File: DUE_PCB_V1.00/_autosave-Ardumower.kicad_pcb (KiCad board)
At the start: 2 copper layers, 169.4 x 95.9 mm, 73 parts, among them J1 9V IN, J10 Sonar_R, J11 Sonar_C, J12 Sonar_L, J13 P_Right, J15 Button, J16 Button, J17 Button, J18 Button, J19 P_Left, J2 I2C0_1, J20 Remote, J21 PCB_2, J22 3.3V, J23 GND, J24 RX & TX, J25 5V IN, J26 Motor Left, J27 Cutter Motor, J28 Motor Right, J29 3.3V IN, J3 I2C0_2, J30 I2C1_2, J4 I2C1_1, J5 Bumper, J6 Drop_Left, J7 Drop_Right, J8 Tilt, J9 Rain, U1 MC33926, U2 MC33926

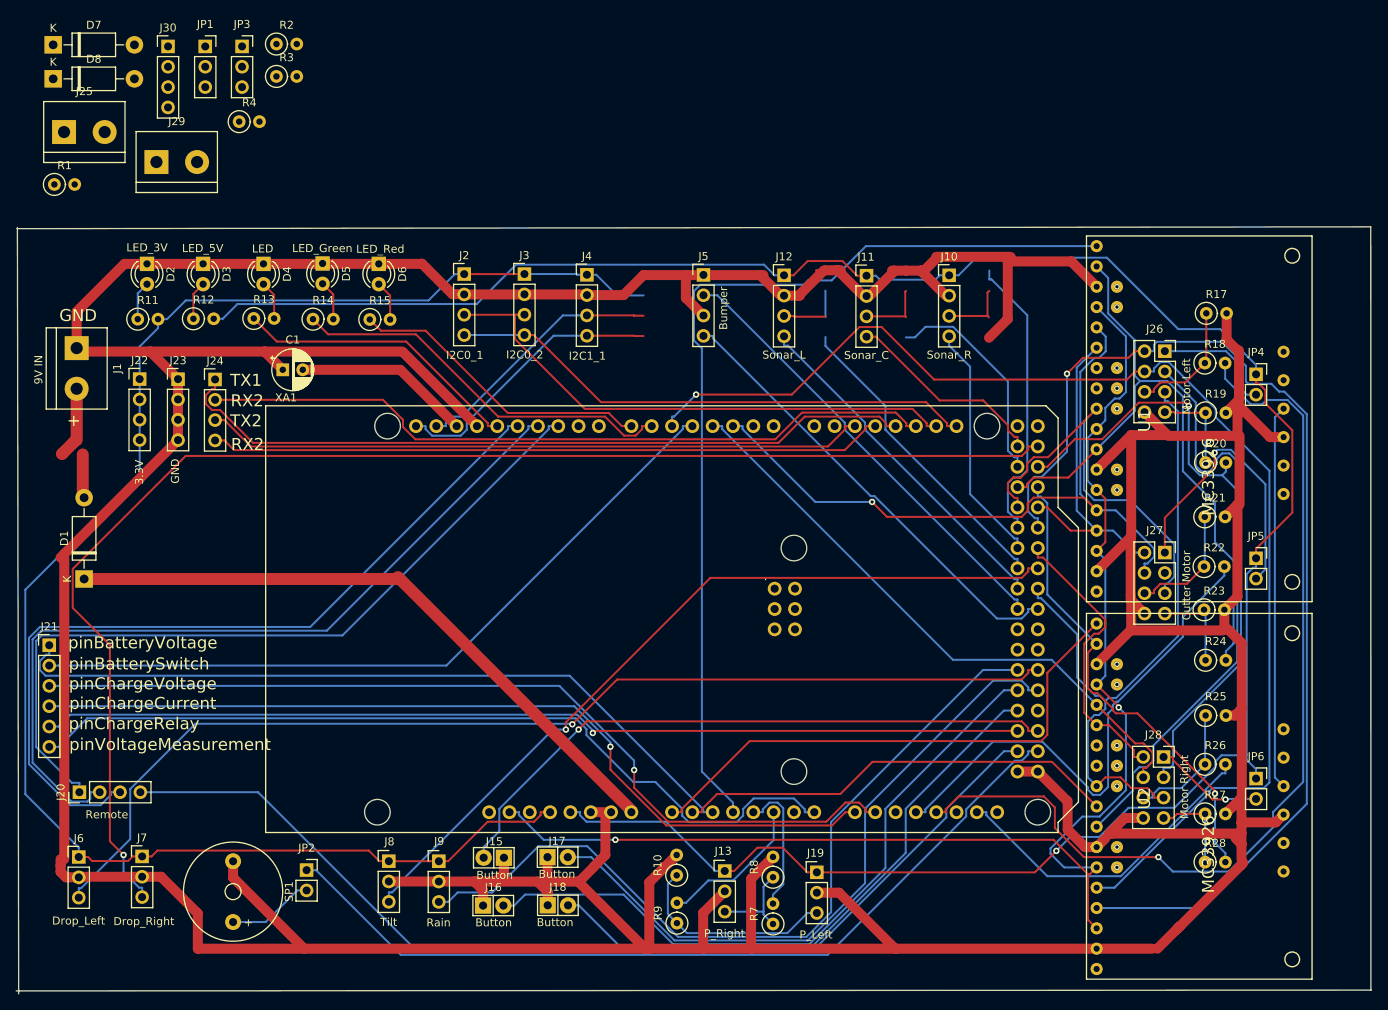
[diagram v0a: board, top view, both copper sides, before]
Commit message: Add Mounting Hole
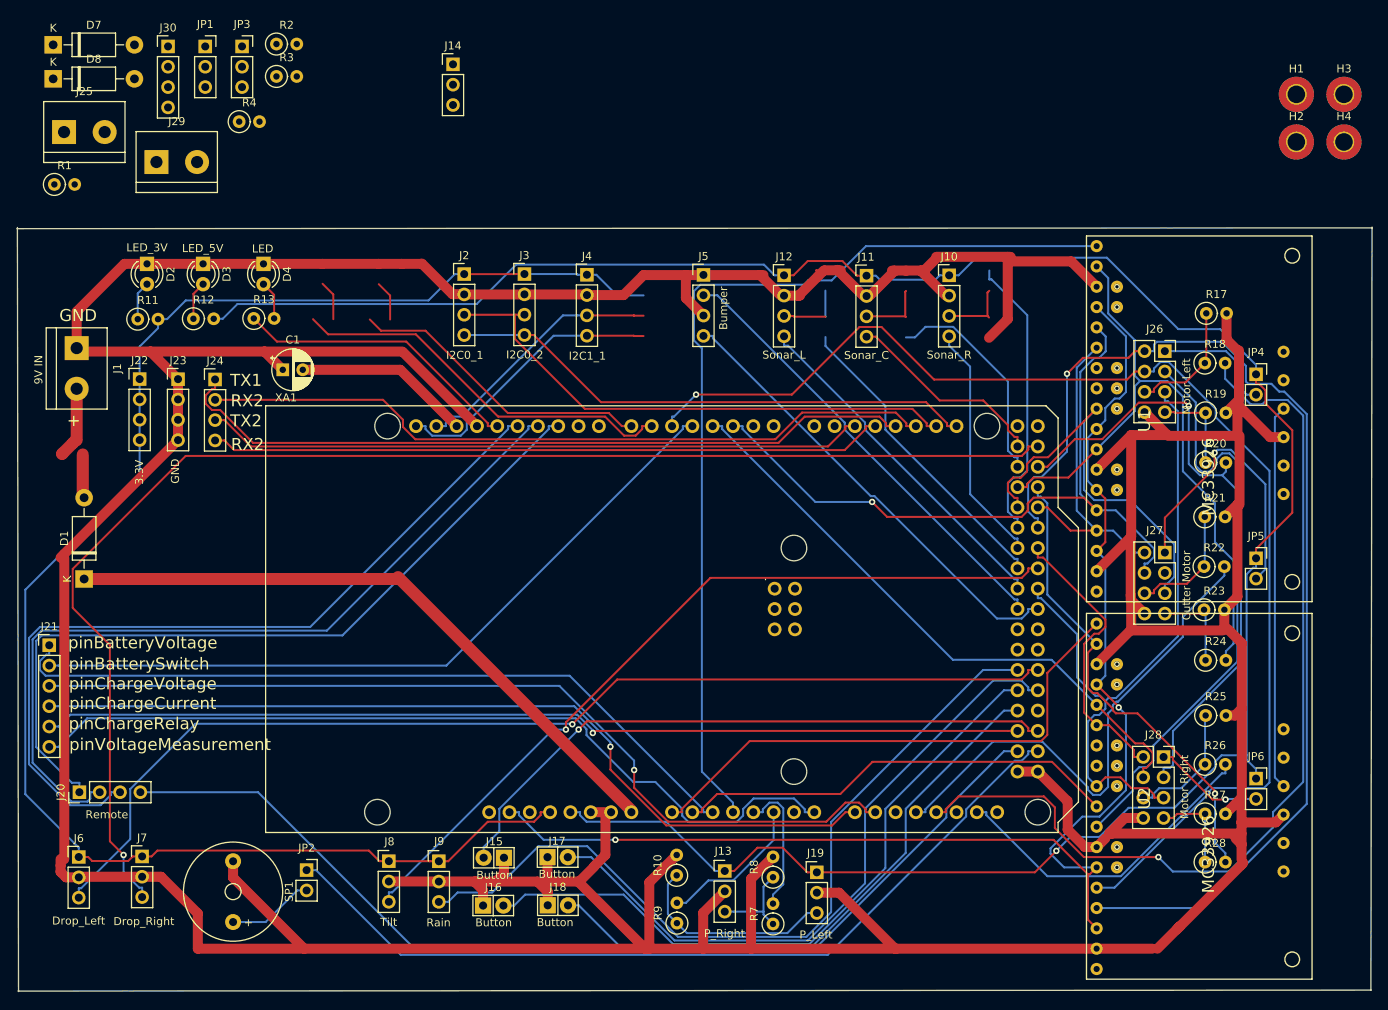
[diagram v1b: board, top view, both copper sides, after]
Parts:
- removed D5: LED_Green, LED_THT:LED_D3.0mm
- removed D6: LED_Red, LED_THT:LED_D3.0mm
- removed R14, R15: 100, Resistor_THT:R_Axial_DIN0207_L6.3mm_D2.5mm_P2.54mm_Vertical
- added H1: MountingHole_Pad, MountingHole:MountingHole_2.2mm_M2_Pad_TopBottom, F.Cu at (198.9, 18.9)
- added H2: MountingHole_Pad, MountingHole:MountingHole_2.2mm_M2_Pad_TopBottom, F.Cu at (198.9, 24.9)
- added H3: MountingHole_Pad, MountingHole:MountingHole_2.2mm_M2_Pad_TopBottom, F.Cu at (204.9, 18.9)
- added H4: MountingHole_Pad, MountingHole:MountingHole_2.2mm_M2_Pad_TopBottom, F.Cu at (204.9, 24.9)
- added J14: Buzzer, Connector_PinHeader_2.54mm:PinHeader_1x03_P2.54mm_Vertical, F.Cu at (93.5, 15.2)
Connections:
- XA1 pad D6: pinGreenLED -> (no net)
- XA1 pad D7: pinRedLED -> (no net)
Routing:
- net (no net): track 0.00 -> 87.3 mm
- net pinGreenLED: track 49.1 -> 0.00 mm
- net pinRedLED: track 38.2 -> 0.00 mm
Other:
- board size 169.4 x 95.9 mm -> 169.4 x 95.6 mm
